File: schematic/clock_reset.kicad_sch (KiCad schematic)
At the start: 36 parts, among them Q2 2N3906, U22 74LS04, U7 74LS05, U8 74LS74, Y1 15.9090Mhz

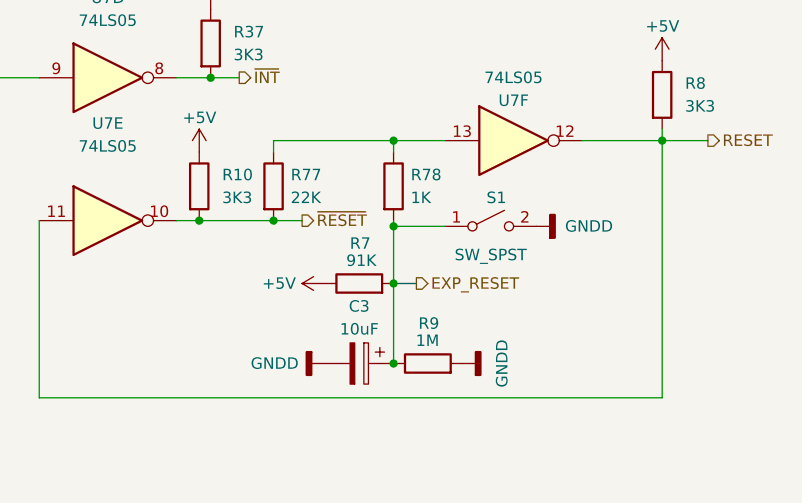
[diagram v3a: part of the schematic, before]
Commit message: RF modulator completed, rough draft complete. Next step is to clean-up all pages.
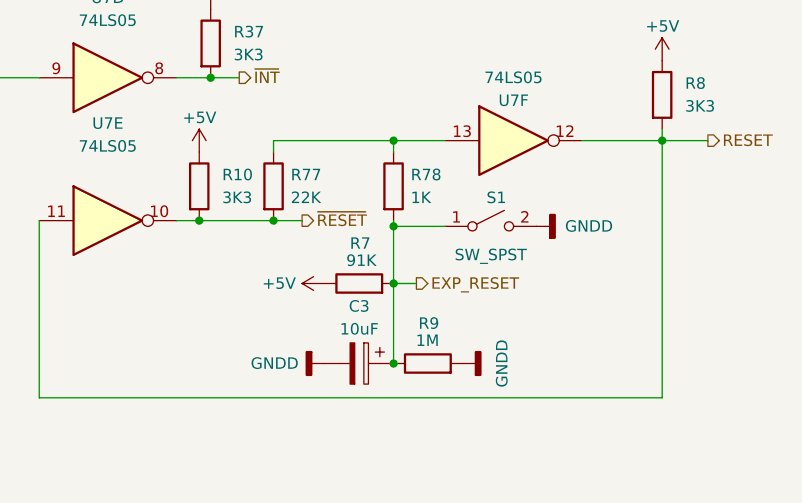
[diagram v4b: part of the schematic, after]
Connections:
- net EXP_RESET: now also C3.1, R7.2, R78.2, R9.1, S1.1 (A)
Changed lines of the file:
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@@
-    (stroke (width 0) (type default) (color 0 0 0 0))
-  )
-  (wire (pts (xy 231.775 135.89) (xy 231.775 144.78))
     (stroke (width 0) (type default) (color 0 0 0 0))
   )
@@
   )
   (wire (pts (xy 186.055 41.275) (xy 186.055 39.37))
+    (stroke (width 0) (type default) (color 0 0 0 0))
+  )
+  (wire (pts (xy 231.775 135.89) (xy 231.775 144.78))
     (stroke (width 0) (type default) (color 0 0 0 0))
   )
@@
     (stroke (width 0) (type default) (color 0 0 0 0))
   )
-  (bus (pts (xy 231.775 135.89) (xy 234.315 135.89))
-    (stroke (width 0) (type default) (color 0 0 0 0))
-  )
   (wire (pts (xy 104.775 113.03) (xy 115.57 113.03))
     (stroke (width 0) (type default) (color 0 0 0 0))
@@
     (stroke (width 0) (type default) (color 0 0 0 0))
   )
+  (wire (pts (xy 231.775 135.89) (xy 234.315 135.89))
+    (stroke (width 0) (type default) (color 0 0 0 0))
+  )

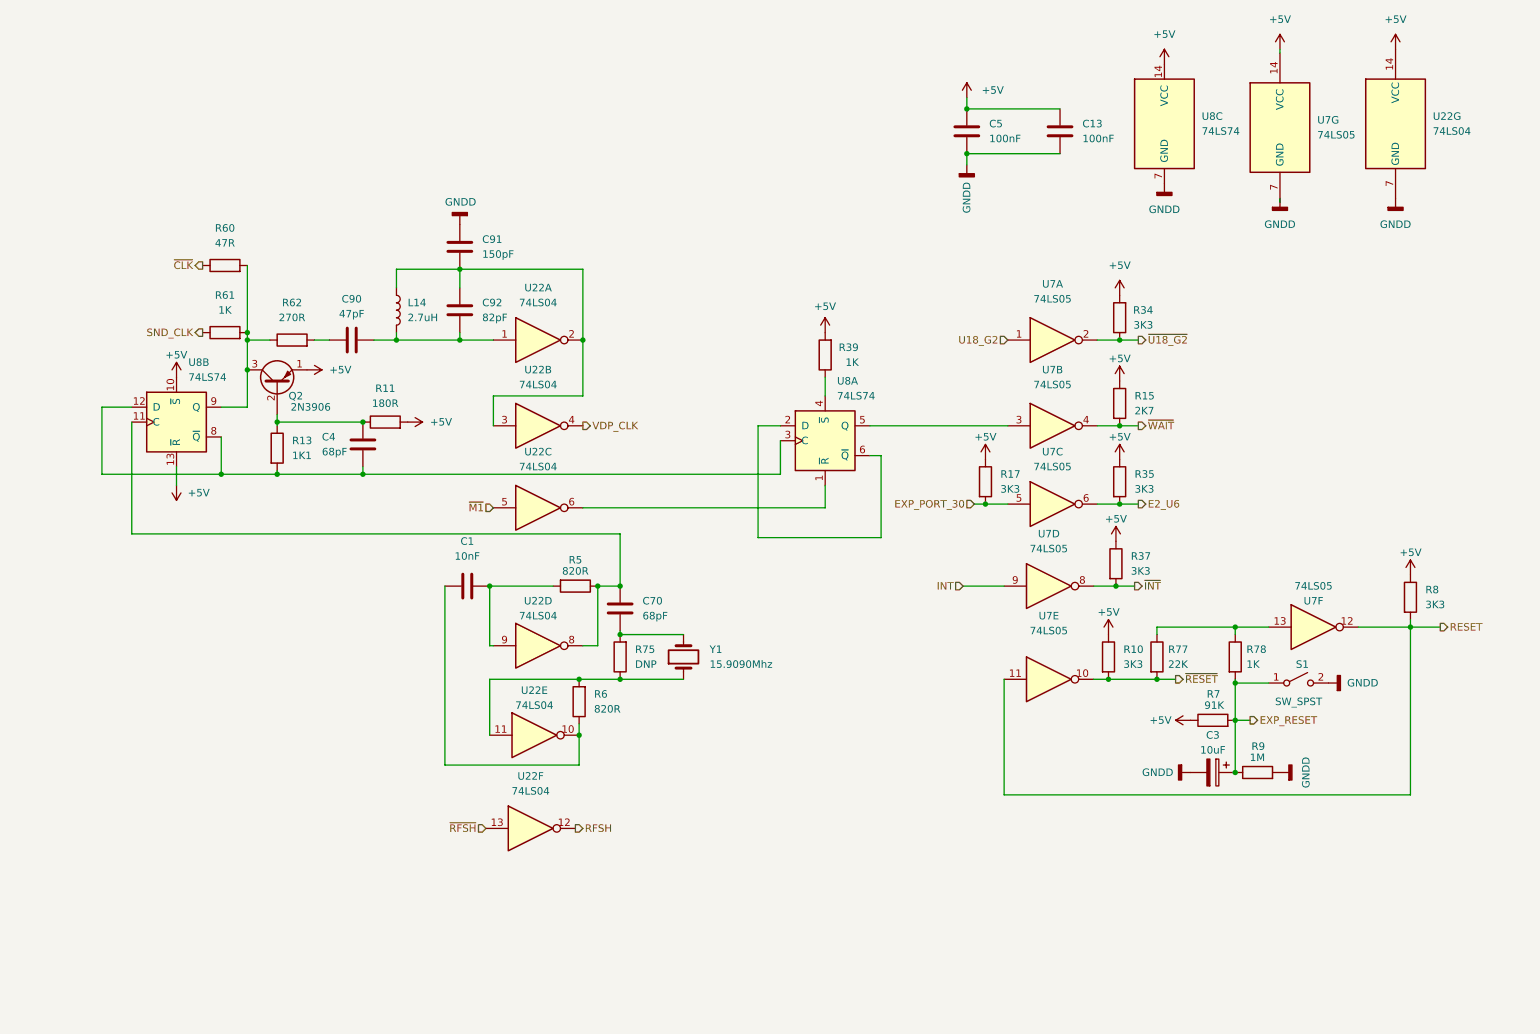
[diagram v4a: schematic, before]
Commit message: Cleanup clock-reset-invert schematic. Checked against wiki.console5.com/wiki/Colecovision. Had a inverter backwards (after cleanup it was obvious since its a standard circuit). Everything else checks, though schematic is missing the wire connection on D8B from 8 to 12. Verified that mine is correct and the wiki is incorrect.
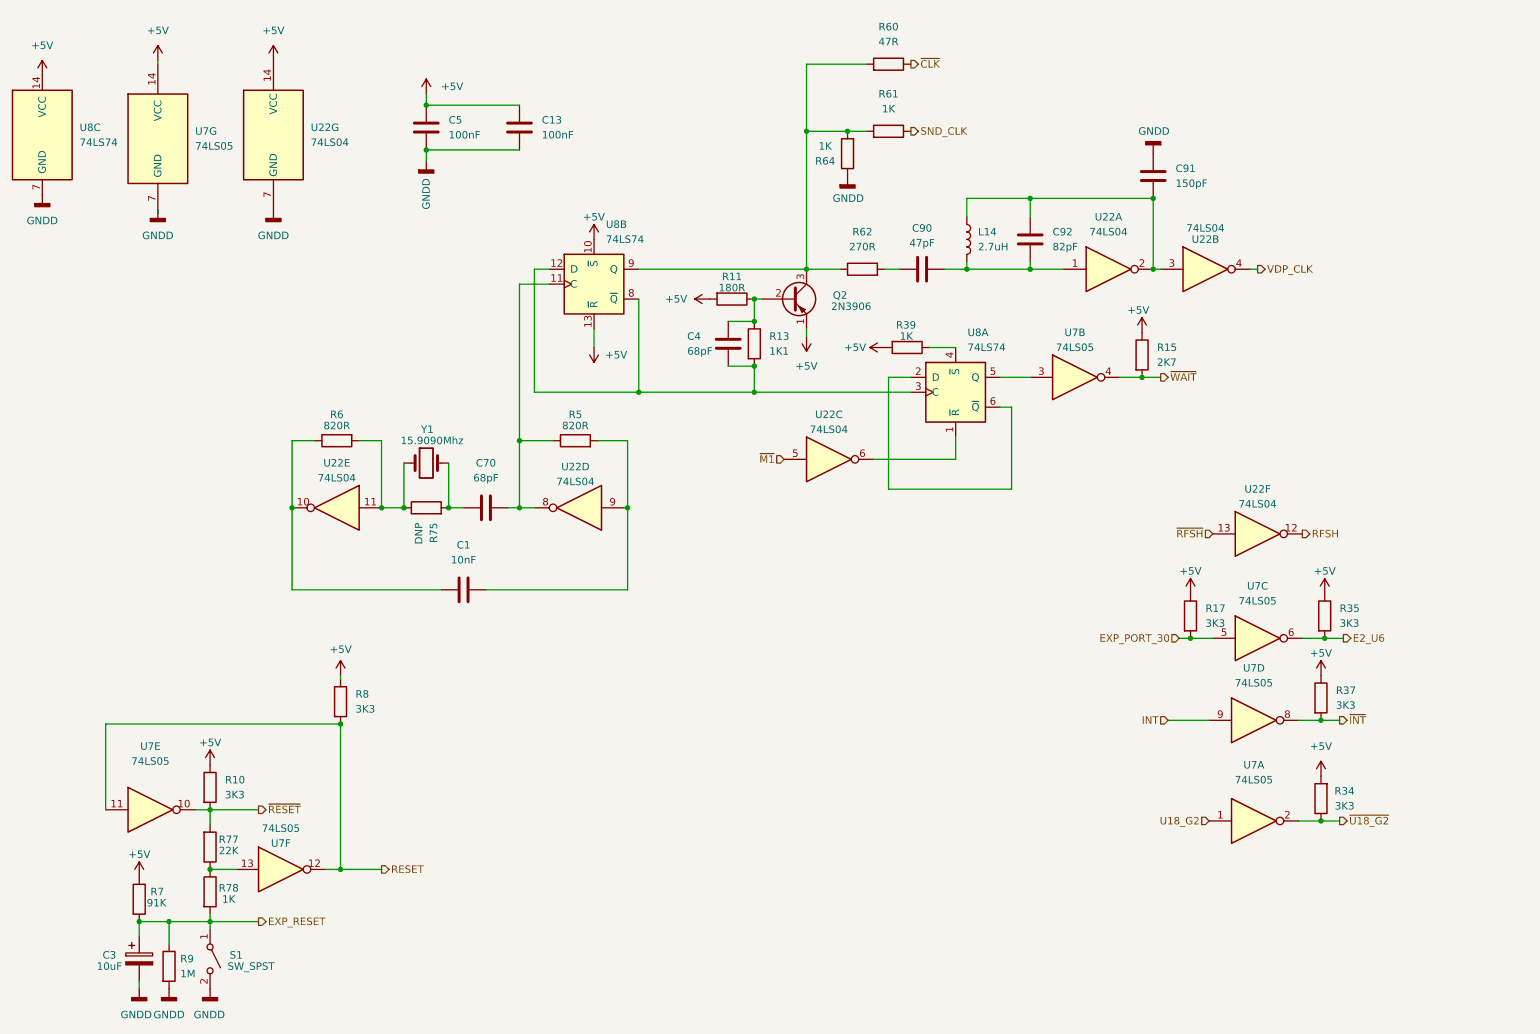
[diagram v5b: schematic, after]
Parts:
- added R64: 1K, symbol Device:R
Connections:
- net GNDD: now also R64.1
- net at Q2.3 (C), R60.2, R61.2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: now also R64.2
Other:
- moved on the sheet: C1, C13, C3, C4, C5, C70, C90, C91, C92, L14, Q2, R10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

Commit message: cleanup on the controller schematic. Checked against wiki.console5.com/wiki/Colecovision. Found a mistake with INT line thanks to the wiki. R21/R22 is reversed between the schematics. Aka R21 is placed on the output of 3. Which actually makes sense, but isn't the way its done on my REV F. R25/R23 match the wiki and that has R25 the pull down on the output pin 6 of the nand. Looks like R21 is a board mistake, but I'll keep it in since its correct for documentation purposes.
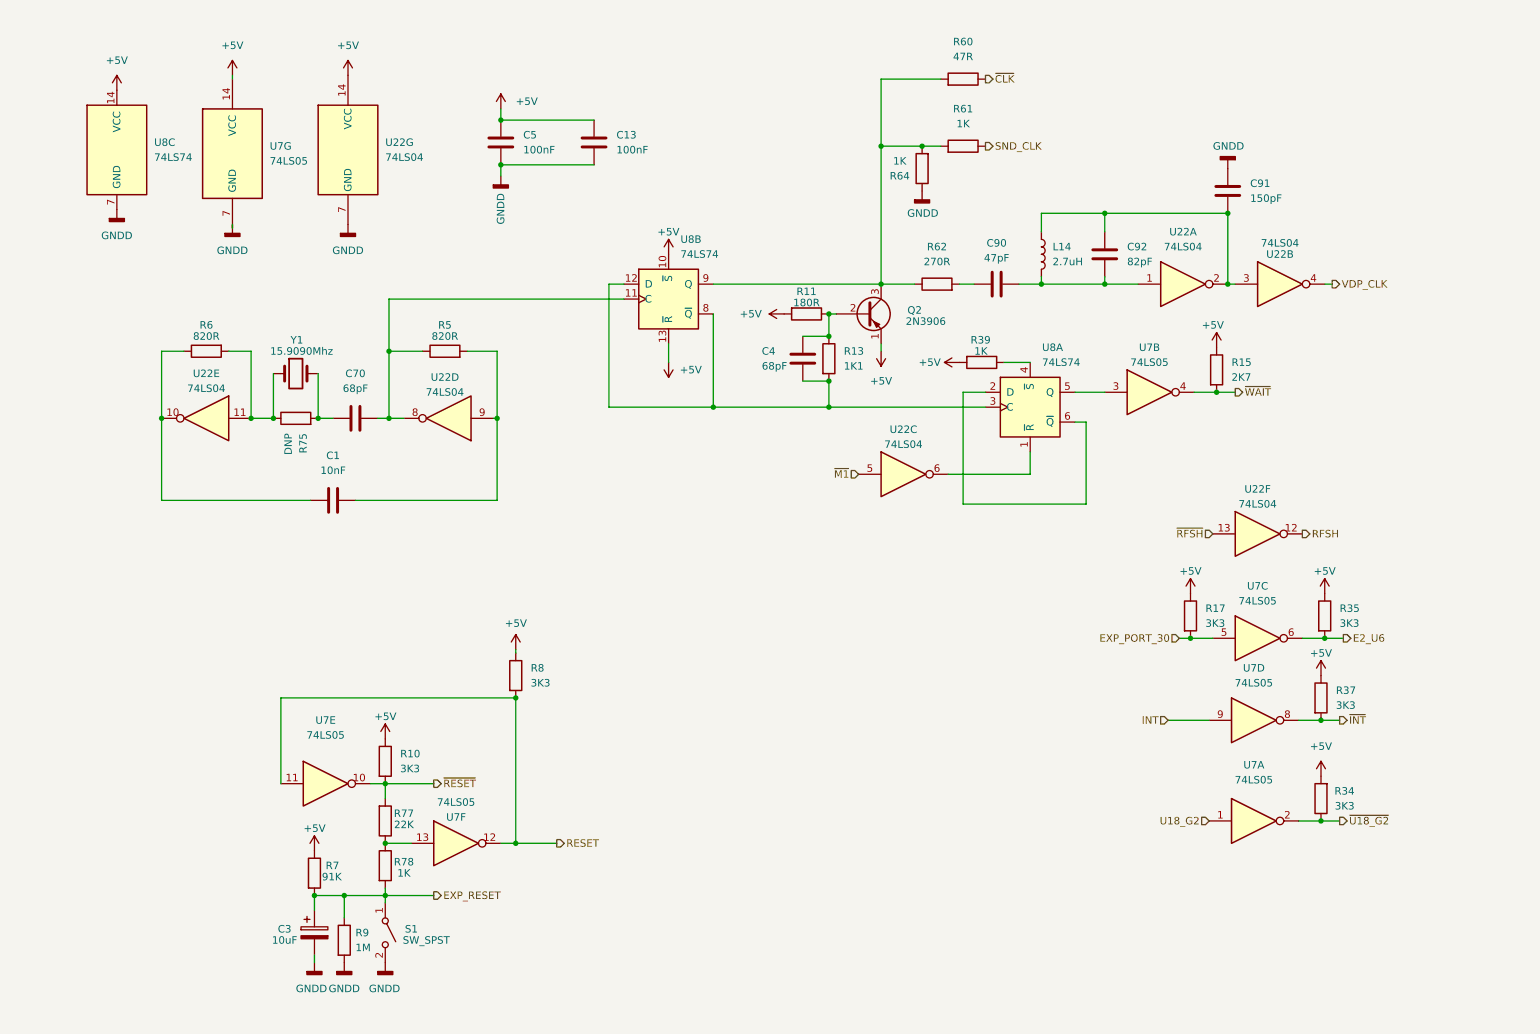
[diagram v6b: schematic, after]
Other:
- moved on the sheet: C1, C13, C3, C4, C5, C70, C90, C91, C92, L14, Q2, R10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

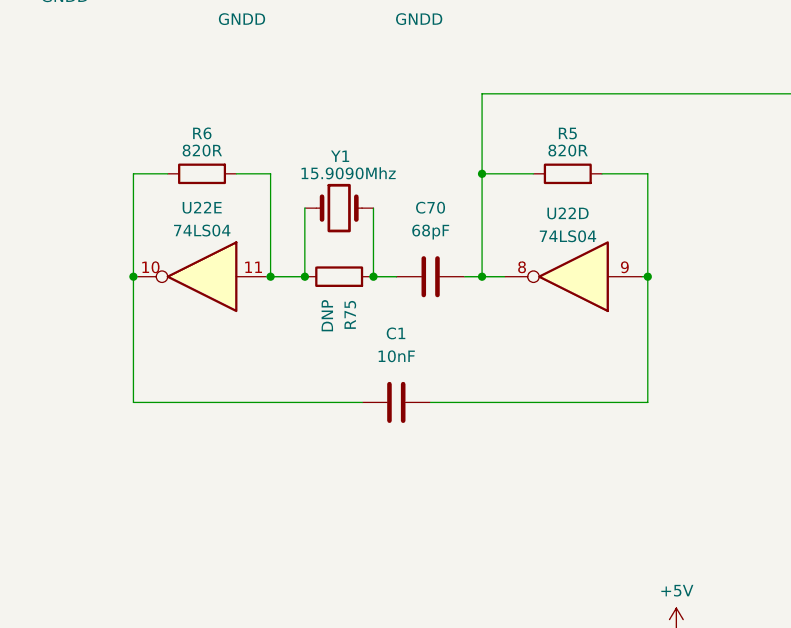
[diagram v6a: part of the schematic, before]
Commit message: cleaned up RF circuit again, and used ChildOfCv schematic as a ref. Fixed a few mistakes. I didn't know his even existed. Its a very nice project. I didn't know it existed till I was googling some sources for the RF part, since the ADAM was different. Though his RF circuit for the daughter board is different in ways that don't make sense for mine. I'll have to double check that by hand.
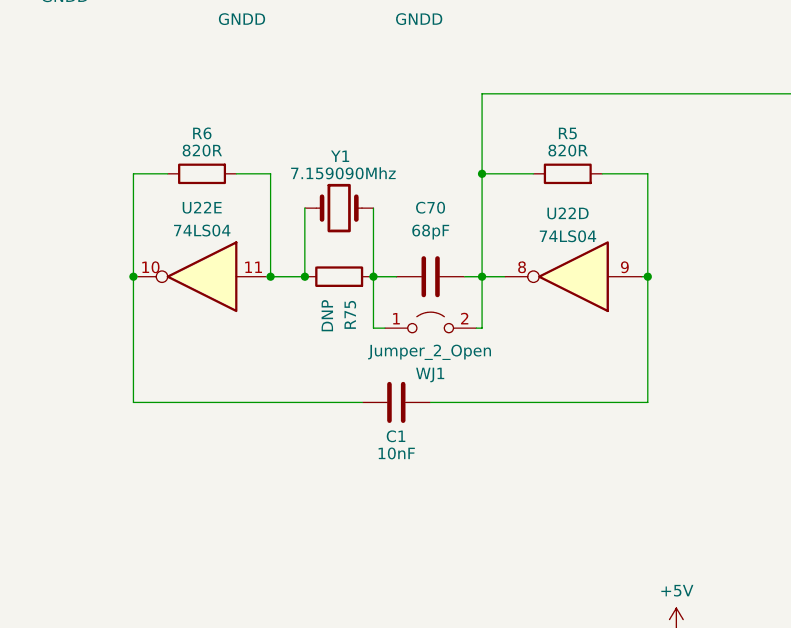
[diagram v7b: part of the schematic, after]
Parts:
- added WJ1: Jumper_2_Open, symbol Jumper:Jumper_2_Open
- Y1: value 15.9090Mhz -> 7.159090Mhz
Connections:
- net at C70.1, R5.1, U22.8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: now also WJ1.2 (B)
- net at C70.2, R75.2, Y1.2: now also WJ1.1 (A)
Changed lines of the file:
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@@
+    (stroke (width 0) (type default) (color 0 0 0 0))
+  )
+  (wire (pts (xy 86.995 90.17) (xy 87.63 90.17))
     (stroke (width 0) (type default) (color 0 0 0 0))
   )
@@
     (stroke (width 0) (type default) (color 0 0 0 0))
   )
+  (wire (pts (xy 87.63 84.455) (xy 87.63 90.17))
+    (stroke (width 0) (type default) (color 0 0 0 0))
+  )
   (wire (pts (xy 106.68 31.75) (xy 106.68 33.655))
     (stroke (width 0) (type default) (color 0 0 0 0))
@@
     (stroke (width 0) (type default) (color 0 0 0 0))
   )
+  (wire (pts (xy 75.565 90.17) (xy 75.565 84.455))
+    (stroke (width 0) (type default) (color 0 0 0 0))
+  )
   (wire (pts (xy 106.68 156.845) (xy 109.22 156.845))
     (stroke (width 0) (type default) (color 0 0 0 0))
@@
   )
   (wire (pts (xy 171.45 38.1) (xy 171.45 61.595))
+    (stroke (width 0) (type default) (color 0 0 0 0))
+  )
+  (wire (pts (xy 76.835 90.17) (xy 75.565 90.17))
     (stroke (width 0) (type default) (color 0 0 0 0))
   )
@@
   )
   (symbol (lib_id "Device:C") (at 78.105 98.425 90) (unit 1)
-    (in_bom yes) (on_board yes) (fields_autoplaced)
-    (property "Reference" "C1" (id 0) (at 78.105 90.805 90))
-    (property "Value" "10nF" (id 1) (at 78.105 93.345 90))
+    (in_bom yes) (on_board yes)
+    (property "Reference" "C1" (id 0) (at 78.105 102.235 90))
+    (property "Value" "10nF" (id 1) (at 78.105 104.14 90))
     (property "Footprint" "" (id 2) (at 81.915 97.4598 0)
       (effects (font (size 1.27 1.27)) hide)
@@
     (pin "7")
   )
+  (symbol (lib_id "Jumper:Jumper_2_Open") (at 81.915 90.17 0) (unit 1)
+    (in_bom yes) (on_board yes)
+    (property "Reference" "WJ1" (id 0) (at 81.915 95.25 0))
+    (property "Value" "Jumper_2_Open" (id 1) (at 81.915 92.71 0))
+    (property "Footprint" "" (id 2) (at 81.915 90.17 0)
+      (effects (font (size 1.27 1.27)) hide)
+    )
+    (property "Datasheet" "~" (id 3) (at 81.915 90.17 0)
+      (effects (font (size 1.27 1.27)) hide)
+    )
+    (pin "1")
+    (pin "2")
+  )
   (symbol (lib_id "power:+5V") (at 135.255 74.93 180) (unit 1)
     (in_bom yes) (on_board yes) (fields_autoplaced)
@@
       (effects (font (size 1.27 1.27)) (justify right))
     )
-    (property "Value" "15.9090Mhz" (id 1) (at 78.105 73.025 0)
+    (property "Value" "7.159090Mhz" (id 1) (at 78.105 73.025 0)
       (effects (font (size 1.27 1.27)) (justify right))
     )

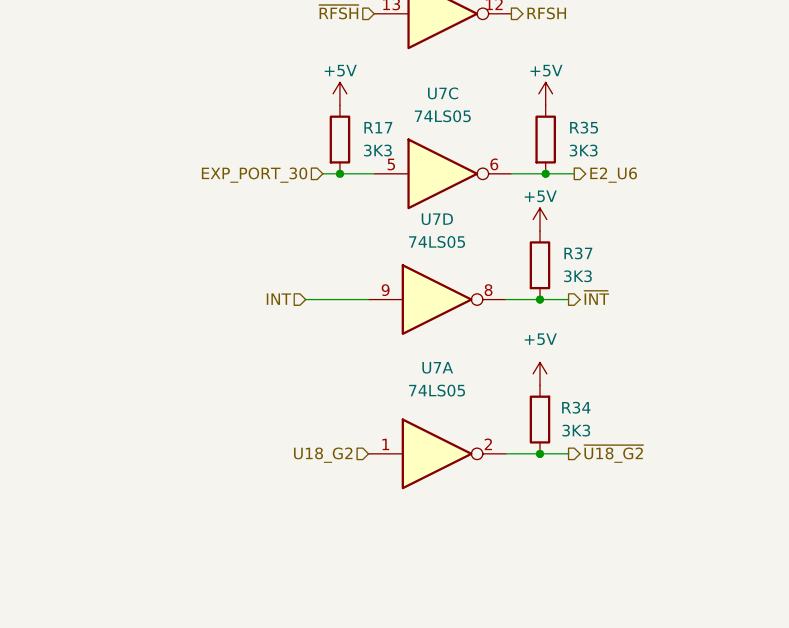
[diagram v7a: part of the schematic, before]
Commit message: all lines renamed, based most of the names from the coleco adam schematic. CS cart lines are my own, and the rest are from the wiki schematic for the controller... those will need to be checked.
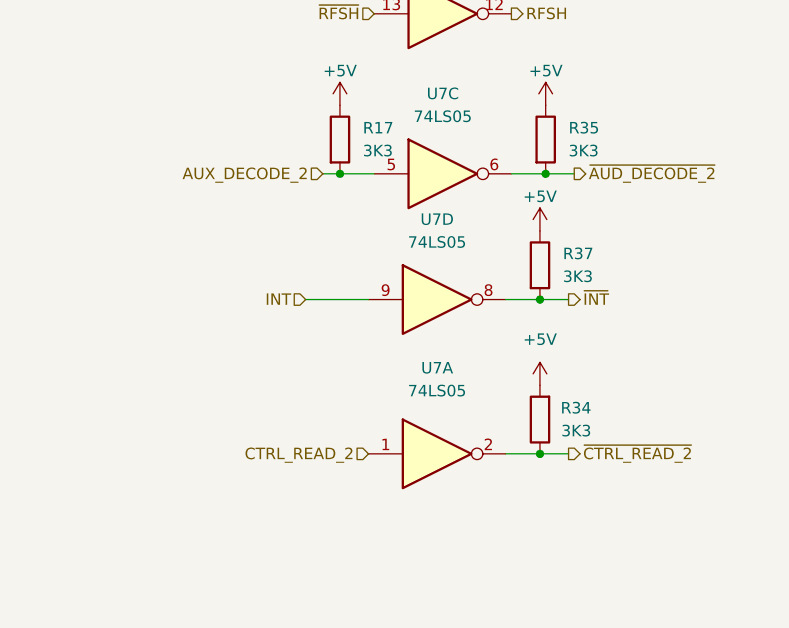
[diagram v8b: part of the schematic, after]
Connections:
- net E2_U6 renamed ~{AUD_DECODE_2}
- net EXP_PORT_30 renamed AUX_DECODE_2
- net U18_G2 renamed CTRL_READ_2
- net ~{U18_G2} renamed ~{CTRL_READ_2}
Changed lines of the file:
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@@
     (stroke (width 0) (type default) (color 0 0 0 0))
   )
-  (hierarchical_label "E2_U6" (shape output) (at 250.19 121.92 0)
+  (hierarchical_label "~{AUD_DECODE_2}" (shape output) (at 250.19 121.92 0)
     (effects (font (size 1.27 1.27)) (justify left))
   )
@@
     (effects (font (size 1.27 1.27)) (justify left))
   )
-  (hierarchical_label "U18_G2" (shape input) (at 227.33 153.035 180)
+  (hierarchical_label "CTRL_READ_2" (shape input) (at 227.33 153.035 180)
     (effects (font (size 1.27 1.27)) (justify right))
   )
@@
     (effects (font (size 1.27 1.27)) (justify left))
   )
-  (hierarchical_label "EXP_PORT_30" (shape input) (at 222.25 121.92 180)
+  (hierarchical_label "AUX_DECODE_2" (shape input) (at 222.25 121.92 180)
     (effects (font (size 1.27 1.27)) (justify right))
   )
@@
     (effects (font (size 1.27 1.27)) (justify left))
   )
-  (hierarchical_label "~{U18_G2}" (shape output) (at 249.555 153.035 0)
+  (hierarchical_label "~{CTRL_READ_2}" (shape output) (at 249.555 153.035 0)
     (effects (font (size 1.27 1.27)) (justify left))
   )
